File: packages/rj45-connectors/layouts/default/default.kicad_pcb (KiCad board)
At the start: 2 copper layers, 3 parts

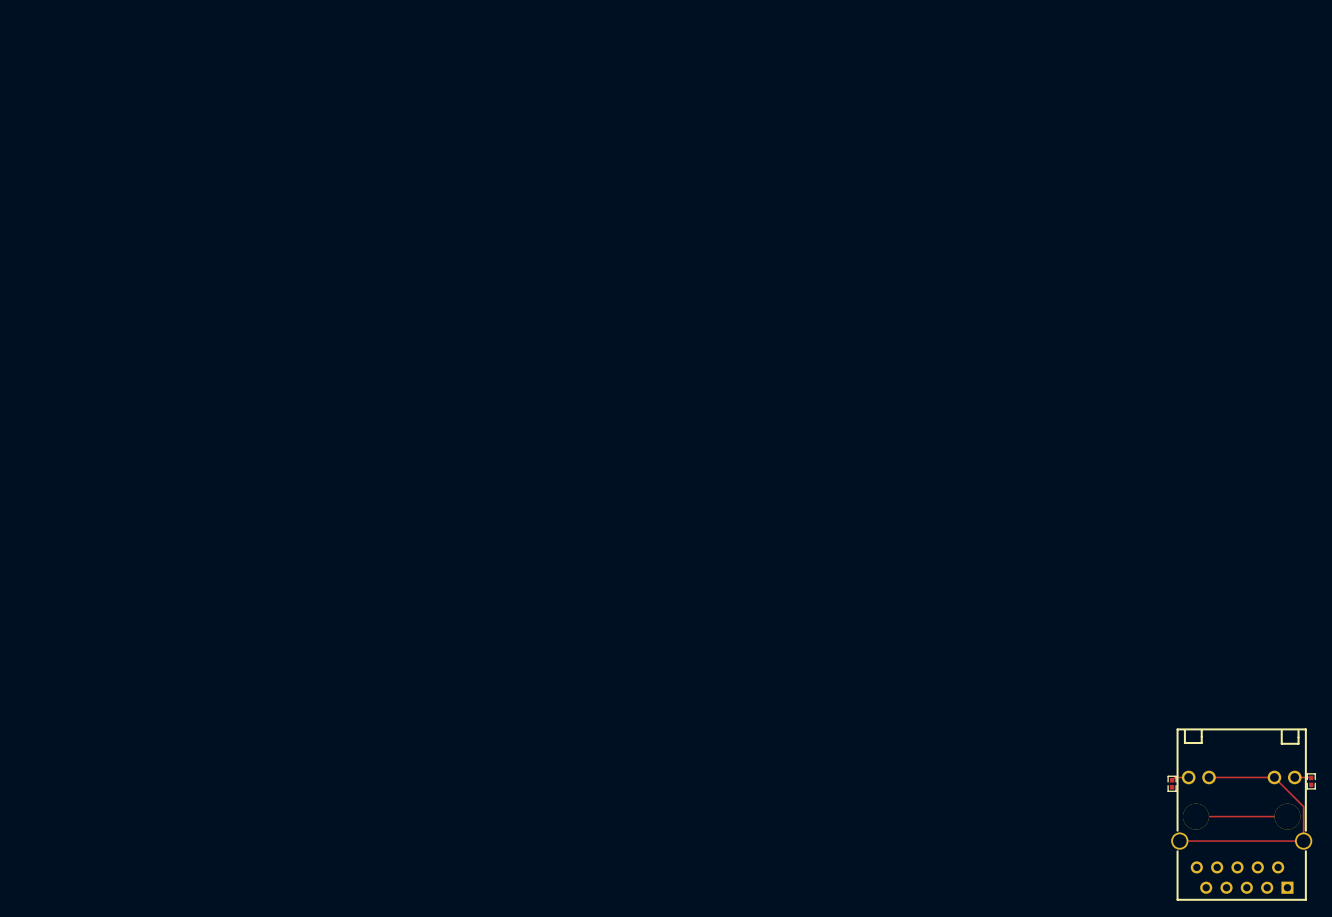
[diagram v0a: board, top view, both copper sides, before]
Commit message: rj45-connectors: fix shorted leds on 8port connector (#206)
* fix led short on 8port build target

* fix inconsistency
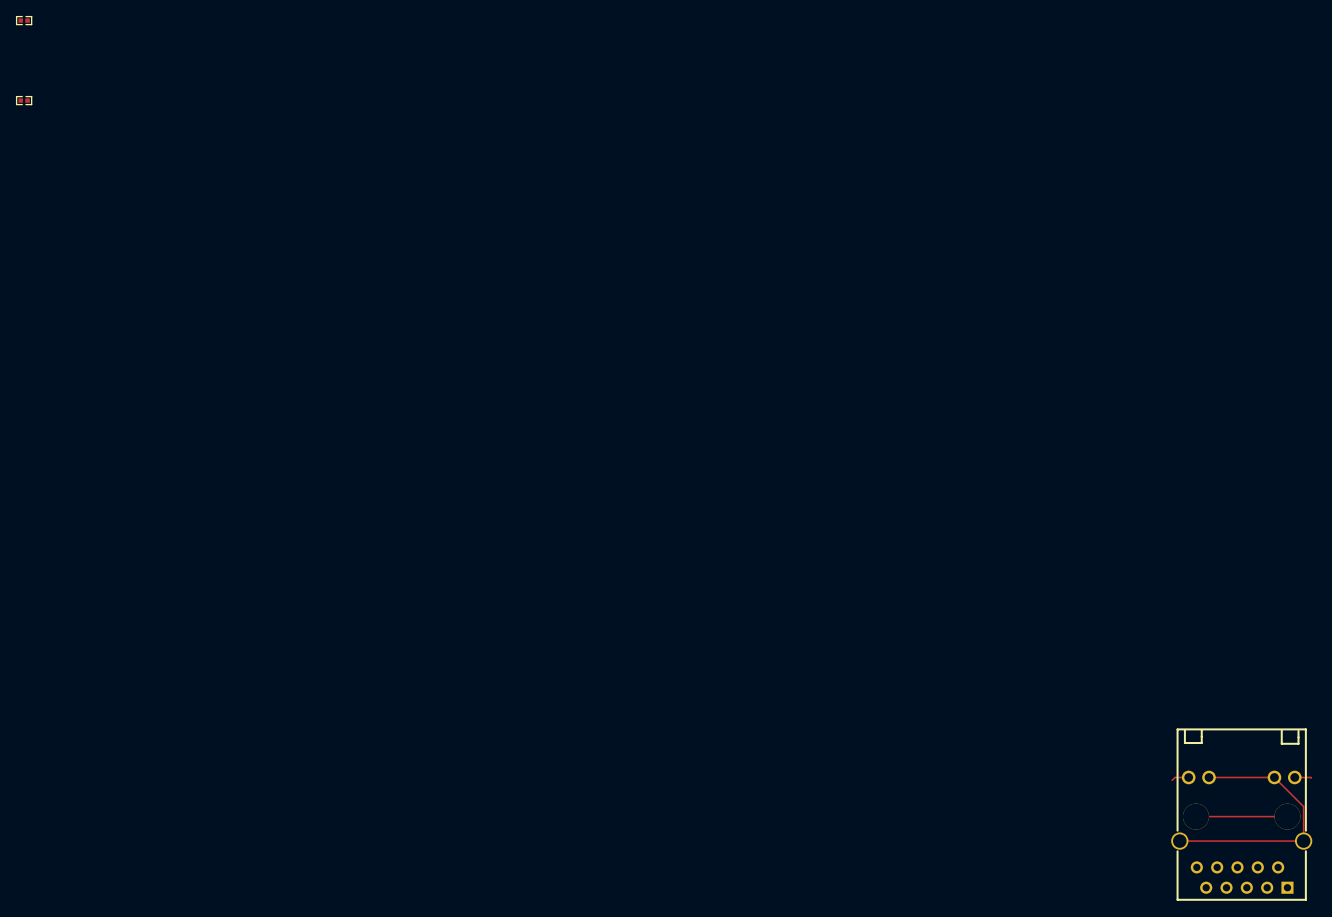
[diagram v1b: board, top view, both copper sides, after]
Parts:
- moved R2 186.9 mm to (0.00, -10.0), turned to 0 degrees
- moved R1 167.0 mm to (0.00, 0.00), turned to 0 degrees
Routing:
- net (no net): track 0.00 -> 48.9 mm
- net GND: track 33.1 -> 0.00 mm
- net net: track 11.4 -> 0.00 mm
- net _14: track 2.22 -> 0.00 mm
- net _11: track 2.09 -> 0.00 mm

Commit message: fix rj45 connectors
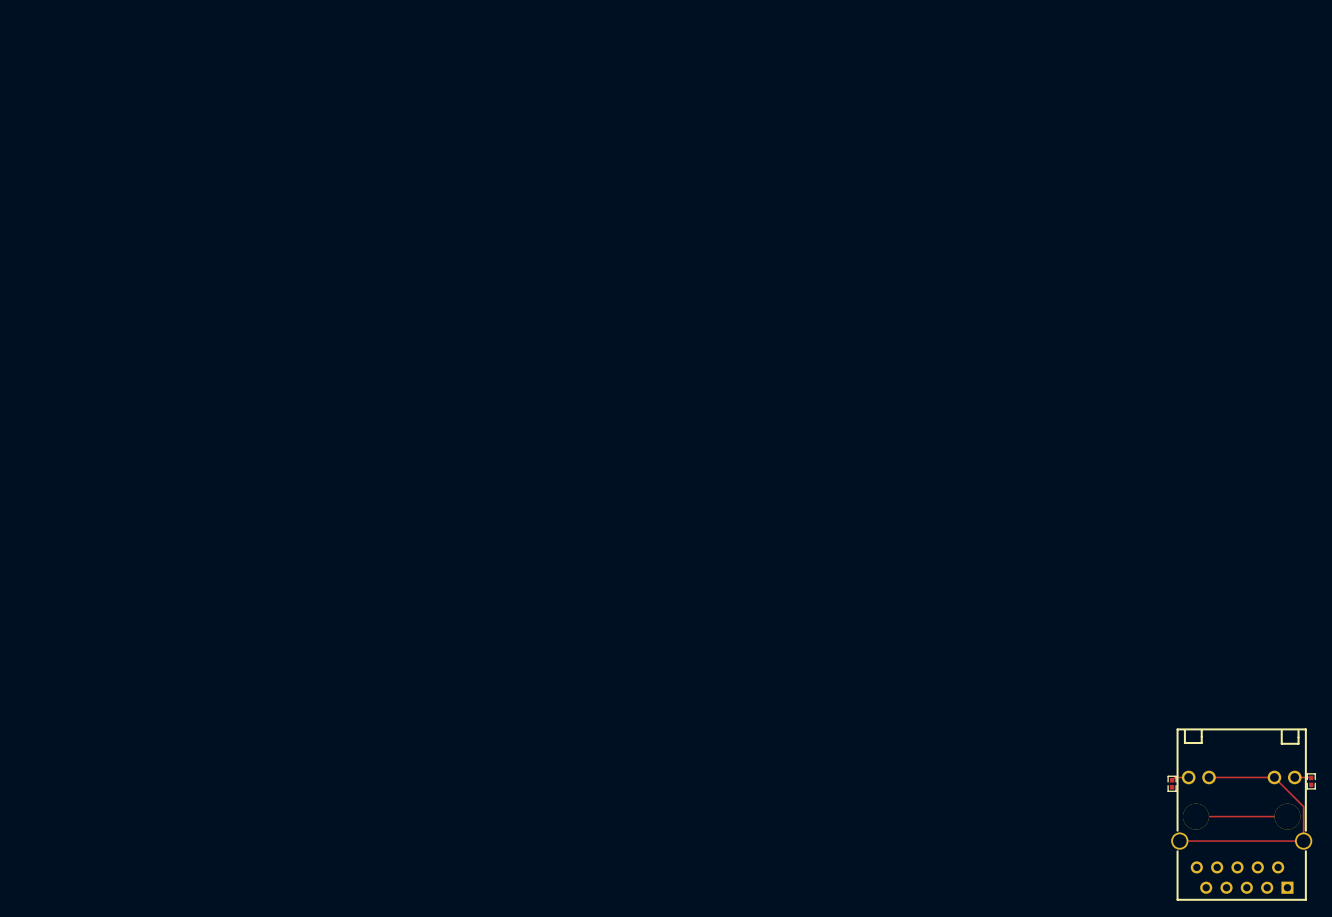
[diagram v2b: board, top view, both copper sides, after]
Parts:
- R1, R2: value 470Ω ±1% 62.5mW -> 470.0Ω
- moved R2 186.9 mm to (160.9, 85.1), turned to 90 degrees
- moved R1 167.0 mm to (143.5, 85.4), turned to 90 degrees
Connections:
- net ETH_LED_LINK renamed ethernet-line-0
- net ETH_LED_SPEED renamed ethernet-line-1
- net ETH_P0_N renamed <bound method has_net_name_affix.get_prefix of <has_net_name_affix '0x1F8110.ethernet.pairs[0].net_name_suffixes[1]' on <Node[Electrical] '0x1F8110.ethernet.pairs[0].n.line'>>>MDI0neg<bound method has...Electrical] '0x1F8110.ethernet.pairs[0].n.line'>>>
- net ETH_P0_P renamed <bound method has_net_name_affix.get_prefix of <has_net_name_affix '0x1F8110.ethernet.pairs[0].net_name_suffixes[0]' on <Node[Electrical] '0x1F8110.ethernet.pairs[0].p.line'>>>MDI0pos<bound method has...Electrical] '0x1F8110.ethernet.pairs[0].p.line'>>>
- net ETH_P1_N renamed <bound method has_net_name_affix.get_prefix of <has_net_name_affix '0x1F8110.ethernet.pairs[1].net_name_suffixes[1]' on <Node[Electrical] '0x1F8110.ethernet.pairs[1].n.line'>>>MDI1neg<bound method has...Electrical] '0x1F8110.ethernet.pairs[1].n.line'>>>
- net ETH_P1_P renamed <bound method has_net_name_affix.get_prefix of <has_net_name_affix '0x1F8110.ethernet.pairs[1].net_name_suffixes[0]' on <Node[Electrical] '0x1F8110.ethernet.pairs[1].p.line'>>>MDI1pos<bound method has...Electrical] '0x1F8110.ethernet.pairs[1].p.line'>>>
- net ETH_P2_N renamed <bound method has_net_name_affix.get_prefix of <has_net_name_affix '0x1F8110.ethernet.pairs[2].net_name_suffixes[1]' on <Node[Electrical] '0x1F8110.ethernet.pairs[2].n.line'>>>MDI2neg<bound method has...Electrical] '0x1F8110.ethernet.pairs[2].n.line'>>>
- net ETH_P2_P renamed <bound method has_net_name_affix.get_prefix of <has_net_name_affix '0x1F8110.ethernet.pairs[2].net_name_suffixes[0]' on <Node[Electrical] '0x1F8110.ethernet.pairs[2].p.line'>>>MDI2pos<bound method has...Electrical] '0x1F8110.ethernet.pairs[2].p.line'>>>
- net ETH_P3_N renamed <bound method has_net_name_affix.get_prefix of <has_net_name_affix '0x1F8110.ethernet.pairs[3].net_name_suffixes[1]' on <Node[Electrical] '0x1F8110.ethernet.pairs[3].n.line'>>>MDI3neg<bound method has...Electrical] '0x1F8110.ethernet.pairs[3].n.line'>>>
- net ETH_P3_P renamed <bound method has_net_name_affix.get_prefix of <has_net_name_affix '0x1F8110.ethernet.pairs[3].net_name_suffixes[0]' on <Node[Electrical] '0x1F8110.ethernet.pairs[3].p.line'>>>MDI3pos<bound method has...Electrical] '0x1F8110.ethernet.pairs[3].p.line'>>>
- net GND renamed ethernet-lv-0
- net _11 renamed 11
- net _14 renamed 14
- U1 pad : net -> (no net)
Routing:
- net (no net): track 48.9 -> 11.4 mm
- net ethernet-lv-0: track 0.00 -> 33.1 mm
- net 14: track 0.00 -> 2.22 mm
- net 11: track 0.00 -> 2.09 mm

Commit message: fix conflict markers in autognerated files
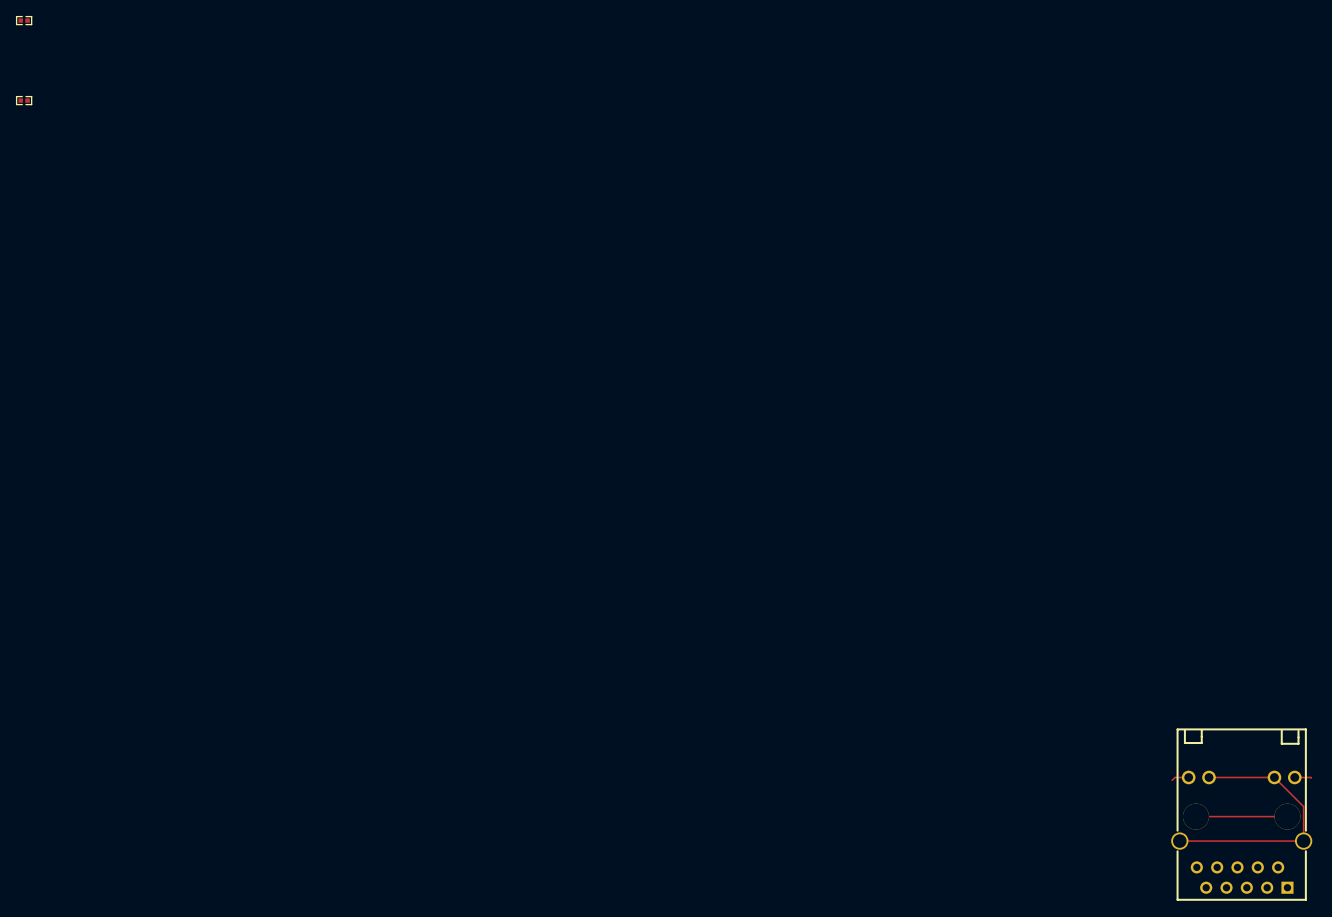
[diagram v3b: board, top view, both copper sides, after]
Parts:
- R1, R2: value 470.0Ω -> 470Ω ±1% 62.5mW
- moved R2 186.9 mm to (0.00, -10.0), turned to 0 degrees
- moved R1 167.0 mm to (0.00, 0.00), turned to 0 degrees
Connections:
- net 11 renamed _11
- net 14 renamed _14
- net <bound method has_net_name_affix.get_prefix of <has_net_name_affix '0x1F8110.ethernet.pairs[0].net_name_suffixes[0]' on <Node[Electrical] '0x1F8110.ethernet.pairs[0].p.line'>>>MDI0pos<bound method has...Electrical] '0x1F8110.ethernet.pairs[0].p.line'>>> renamed ETH_P0_P
- net <bound method has_net_name_affix.get_prefix of <has_net_name_affix '0x1F8110.ethernet.pairs[0].net_name_suffixes[1]' on <Node[Electrical] '0x1F8110.ethernet.pairs[0].n.line'>>>MDI0neg<bound method has...Electrical] '0x1F8110.ethernet.pairs[0].n.line'>>> renamed ETH_P0_N
- net <bound method has_net_name_affix.get_prefix of <has_net_name_affix '0x1F8110.ethernet.pairs[1].net_name_suffixes[0]' on <Node[Electrical] '0x1F8110.ethernet.pairs[1].p.line'>>>MDI1pos<bound method has...Electrical] '0x1F8110.ethernet.pairs[1].p.line'>>> renamed ETH_P1_P
- net <bound method has_net_name_affix.get_prefix of <has_net_name_affix '0x1F8110.ethernet.pairs[1].net_name_suffixes[1]' on <Node[Electrical] '0x1F8110.ethernet.pairs[1].n.line'>>>MDI1neg<bound method has...Electrical] '0x1F8110.ethernet.pairs[1].n.line'>>> renamed ETH_P1_N
- net <bound method has_net_name_affix.get_prefix of <has_net_name_affix '0x1F8110.ethernet.pairs[2].net_name_suffixes[0]' on <Node[Electrical] '0x1F8110.ethernet.pairs[2].p.line'>>>MDI2pos<bound method has...Electrical] '0x1F8110.ethernet.pairs[2].p.line'>>> renamed ETH_P2_P
- net <bound method has_net_name_affix.get_prefix of <has_net_name_affix '0x1F8110.ethernet.pairs[2].net_name_suffixes[1]' on <Node[Electrical] '0x1F8110.ethernet.pairs[2].n.line'>>>MDI2neg<bound method has...Electrical] '0x1F8110.ethernet.pairs[2].n.line'>>> renamed ETH_P2_N
- net <bound method has_net_name_affix.get_prefix of <has_net_name_affix '0x1F8110.ethernet.pairs[3].net_name_suffixes[0]' on <Node[Electrical] '0x1F8110.ethernet.pairs[3].p.line'>>>MDI3pos<bound method has...Electrical] '0x1F8110.ethernet.pairs[3].p.line'>>> renamed ETH_P3_P
- net <bound method has_net_name_affix.get_prefix of <has_net_name_affix '0x1F8110.ethernet.pairs[3].net_name_suffixes[1]' on <Node[Electrical] '0x1F8110.ethernet.pairs[3].n.line'>>>MDI3neg<bound method has...Electrical] '0x1F8110.ethernet.pairs[3].n.line'>>> renamed ETH_P3_N
- net ethernet-line-0 renamed ETH_LED_LINK
- net ethernet-line-1 renamed ETH_LED_SPEED
- net ethernet-lv-0 renamed GND
- U1 pad : (no net) -> net
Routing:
- net (no net): track 11.4 -> 48.9 mm
- net GND: track 33.1 -> 0.00 mm
- net _14: track 2.22 -> 0.00 mm
- net _11: track 2.09 -> 0.00 mm

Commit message: update parts
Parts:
- R1, R2: value 470Ω ±1% 62.5mW -> 470±5.0%Ω
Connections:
- net ETH_P0_N renamed ETH_N0_N
- net ETH_P1_N renamed ETH_N1_N
- net ETH_P2_N renamed ETH_N2_N
- net ETH_P3_N renamed ETH_N3_N
- net GND renamed lv
- net _11 renamed 11
- net _14 renamed 14
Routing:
- net 0: track 0.00 -> 48.9 mm
- net (no net): track 48.9 -> 0.00 mm
